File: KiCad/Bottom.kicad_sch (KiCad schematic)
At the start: 36 parts, among them U101 SS54_C22452, U102 EC12E1220813, U103 RaspberryPi_Pico, U104 TS-1187A-B-A-B, U105 TS-1187A-B-A-B, U179 74HC14D,653, U180 AO3400A

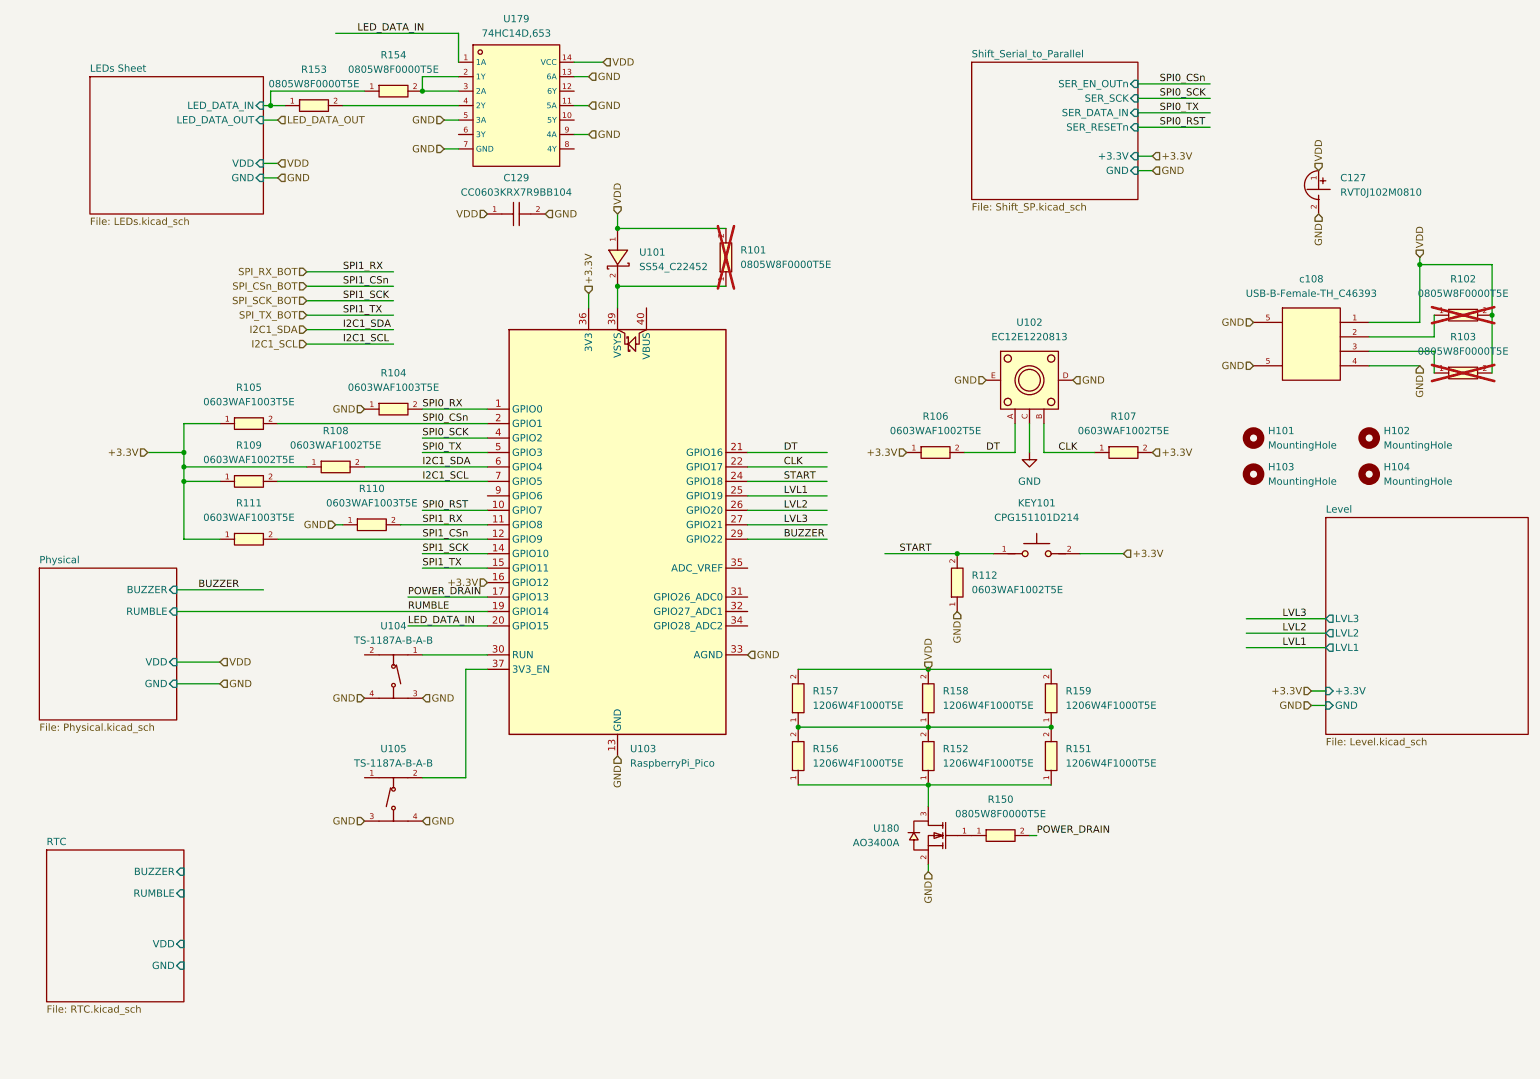
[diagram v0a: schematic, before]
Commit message: Updated to not use adressable LED. Sch only
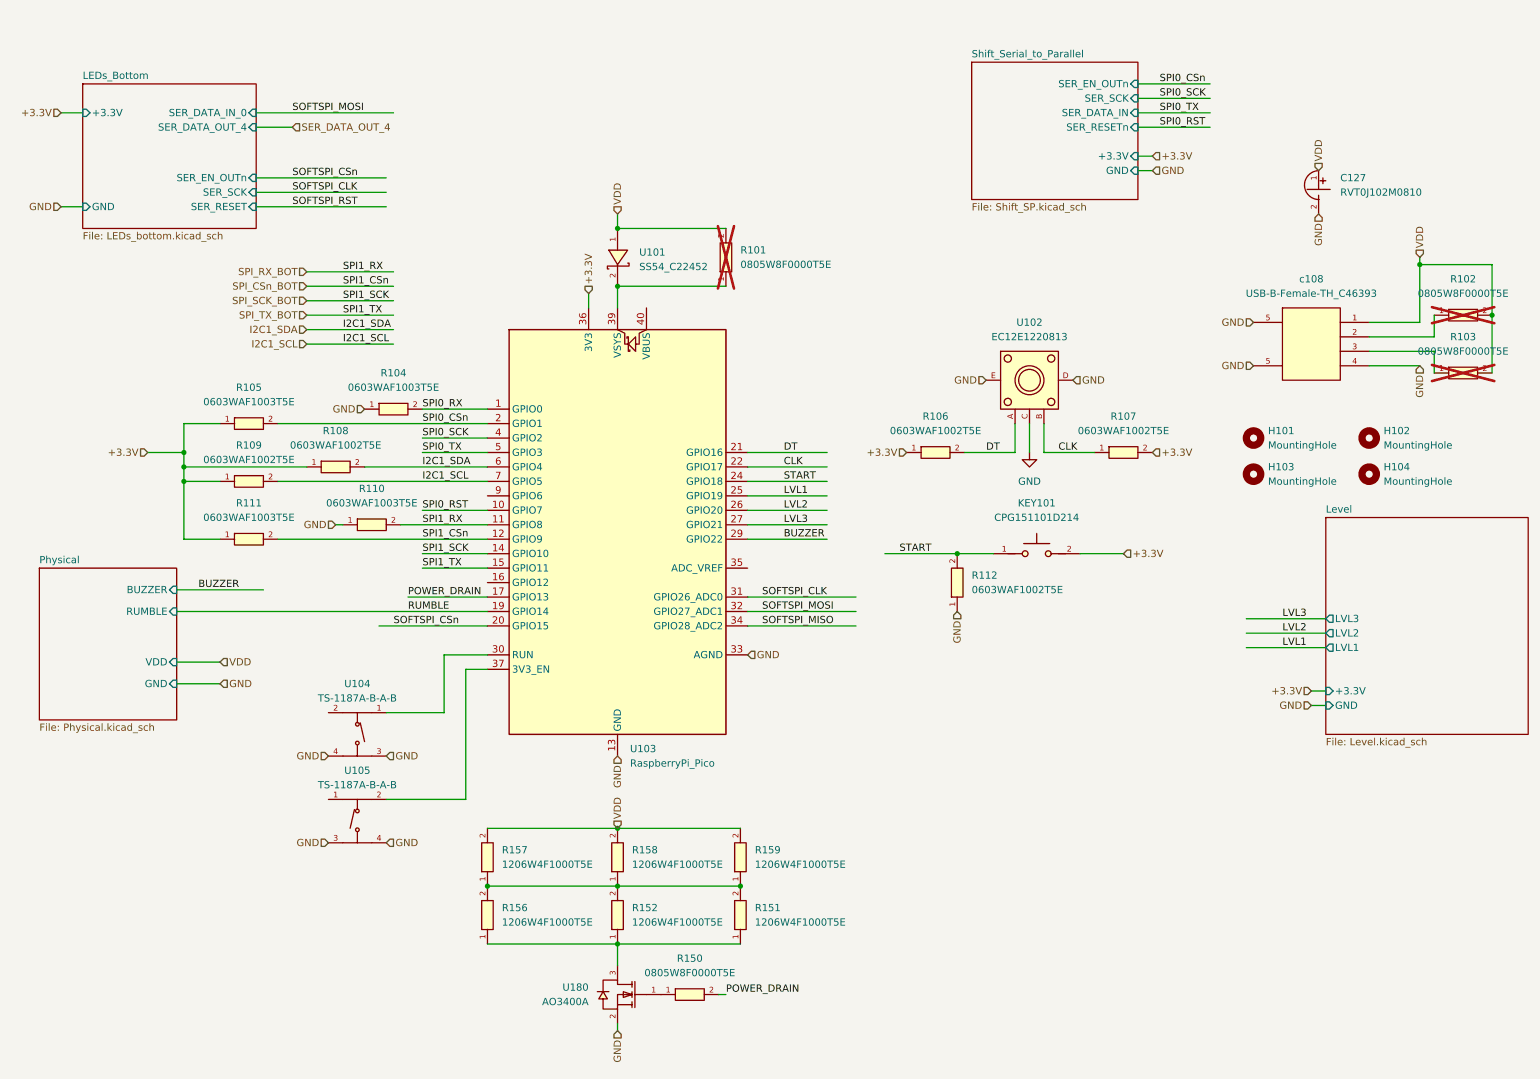
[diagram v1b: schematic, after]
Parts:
- removed C129: CC0603KRX7R9BB104, footprint:C0603, symbol CC0603KRX7R9BB104:CC0603KRX7R9BB104
- removed R153, R154: 0805W8F0000T5E, footprint:R0805, symbol 0805W8F0000T5E:0805W8F0000T5E
- removed U179: 74HC14D,653, footprint:SOIC-14_L8.7-W3.9-P1.27-LS6.0-BL, symbol 74HC14D,653:74HC14D,653
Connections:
- net +3.3V: no longer U103.16 (GPIO12)
- net SOFTSPI_CLK: now reaches U103.31 (GPIO26_ADC0)
- net SOFTSPI_MOSI: now reaches U103.32 (GPIO27_ADC1)
- net SOFTSPI_MISO: now reaches U103.34 (GPIO28_ADC2)
- net LED_DATA_IN renamed SOFTSPI_CSn
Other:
- removed sheet LEDs Sheet
- removed sheet RTC
- added sheet LEDs_Bottom (LEDs_bottom.kicad_sch)
- moved on the sheet: R150, R151, R152, R156, R157, R158, R159, U104, U105, U180

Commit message: Ready for PCB layout with discreet LEDs
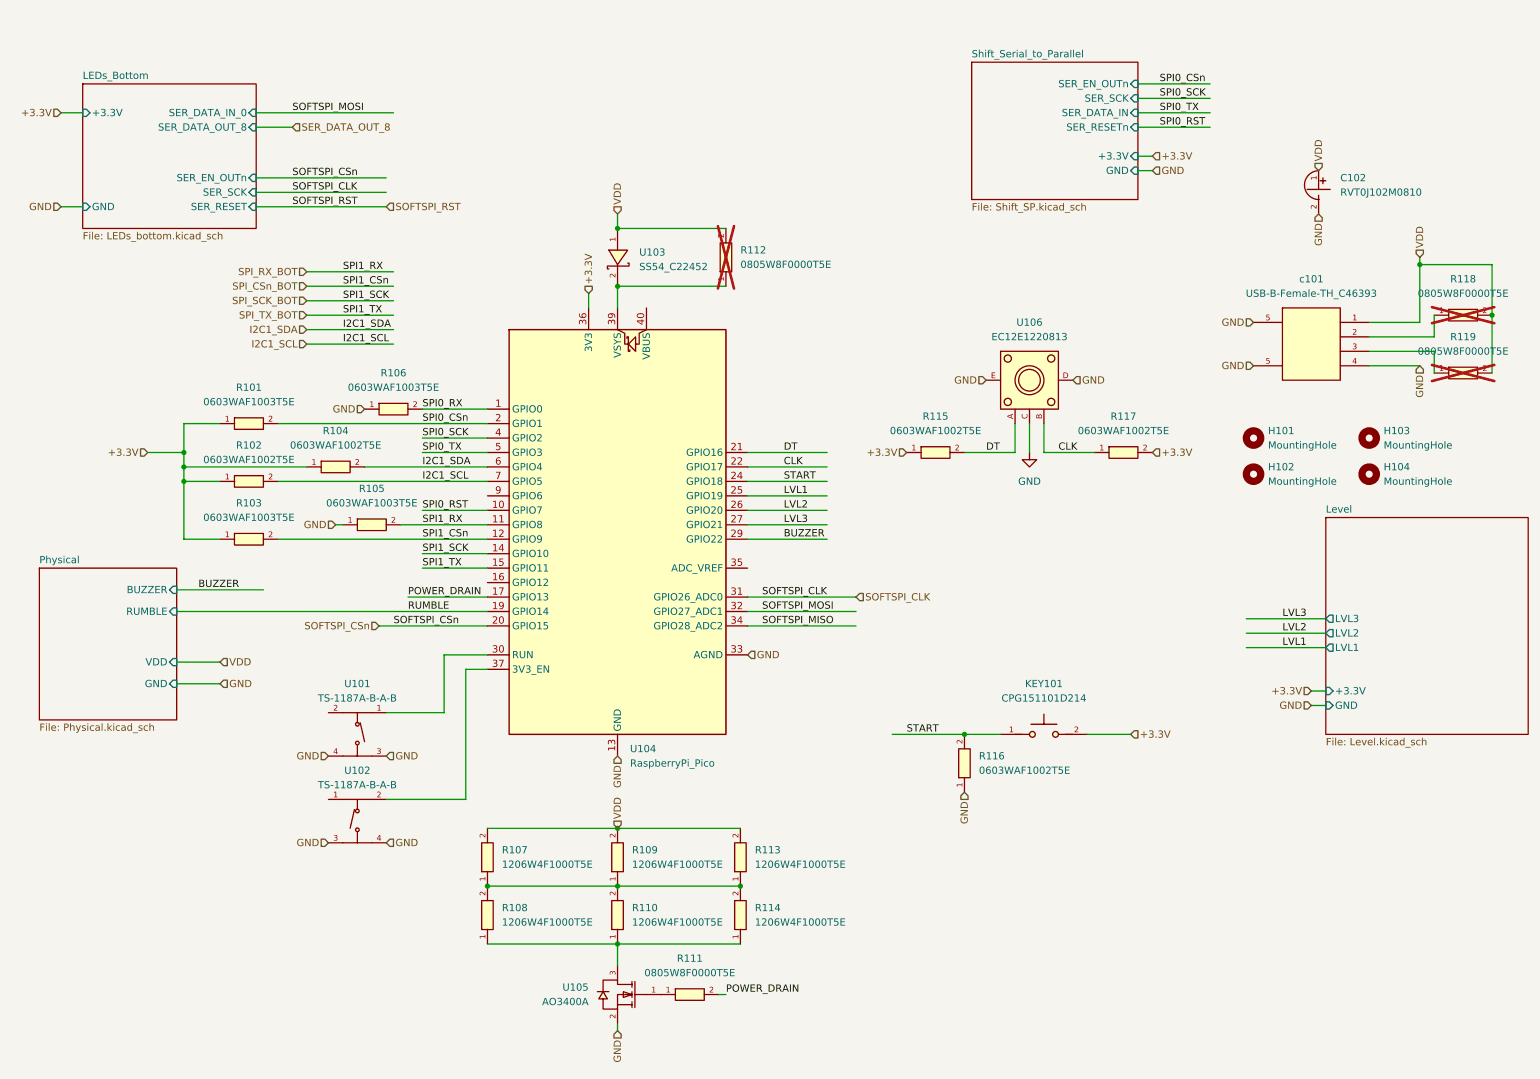
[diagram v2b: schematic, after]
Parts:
- renumbered C127 to C102, H103 to H102, H102 to H103, R105 to R101, R109 to R102, R111 to R103, R108 to R104, R110 to R105, R104 to R106, R157 to R107, R156 to R108, R158 to R109, R152 to R110, R150 to R111, R101 to R112, R159 to R113, R151 to R114, R106 to R115, R112 to R116, R107 to R117, R102 to R118, R103 to R119, U104 to U101, U105 to U102, U101 to U103, U103 to U104, U180 to U105, U102 to U106, c108 to c101
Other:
- sheet LEDs_Bottom ports: added SER_DATA_OUT_8; removed SER_DATA_OUT_4
- moved on the sheet: KEY101, R116
